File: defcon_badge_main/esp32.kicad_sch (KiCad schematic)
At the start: 15 parts, among them J1 USB_C_Receptacle, SW1 Push_Button, SW2 Push_Button, U3 ESP32-C5-WROOM-1U

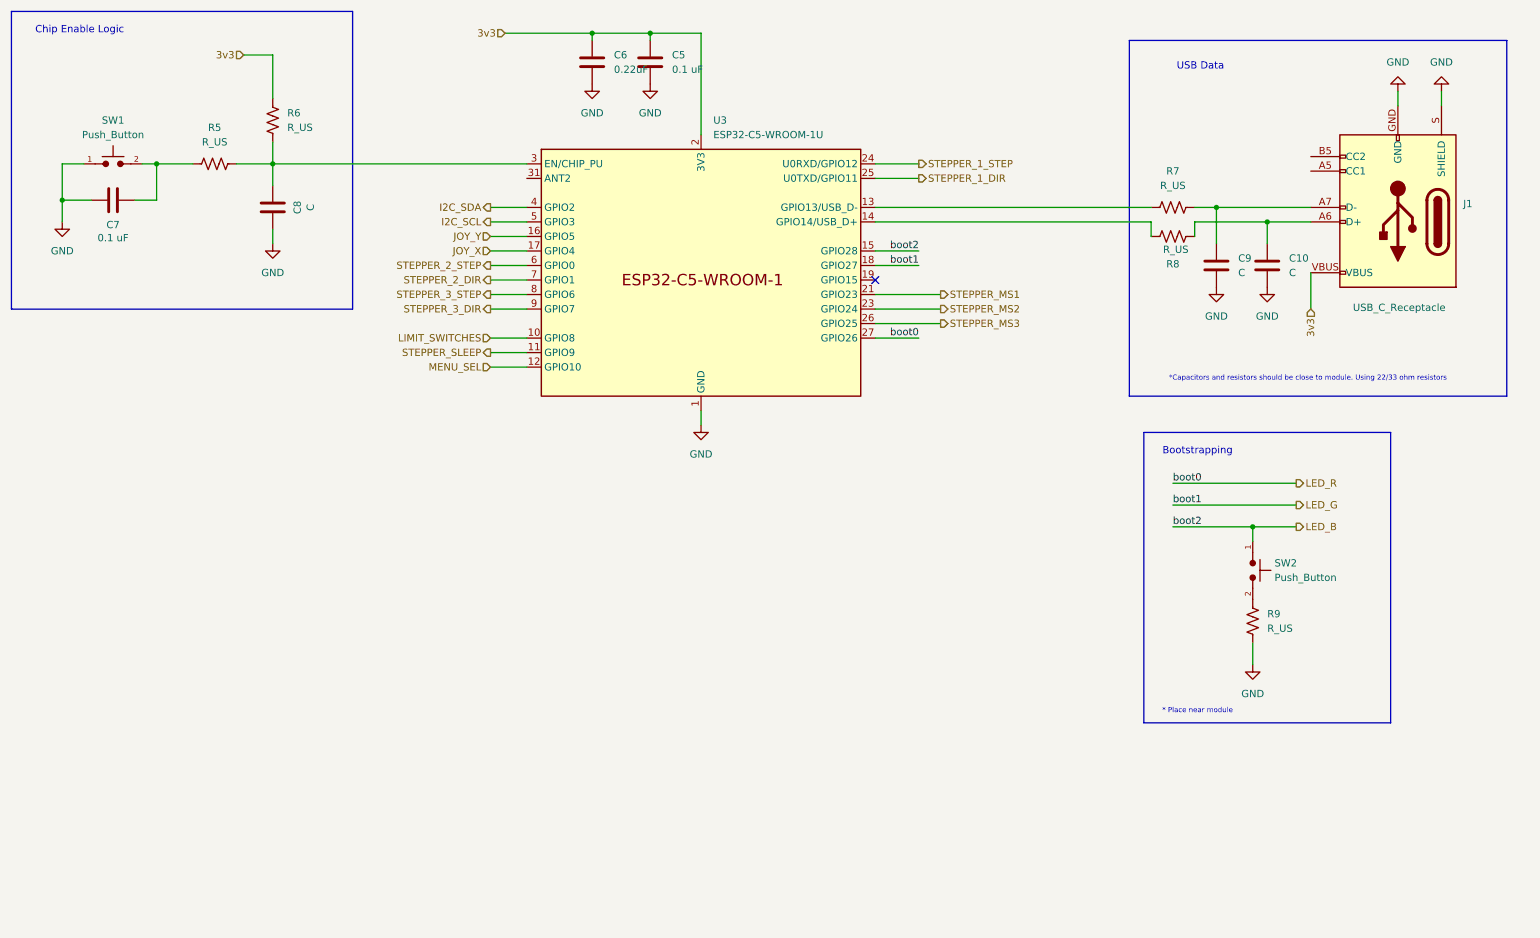
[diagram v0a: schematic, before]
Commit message: ESP32 test board layout
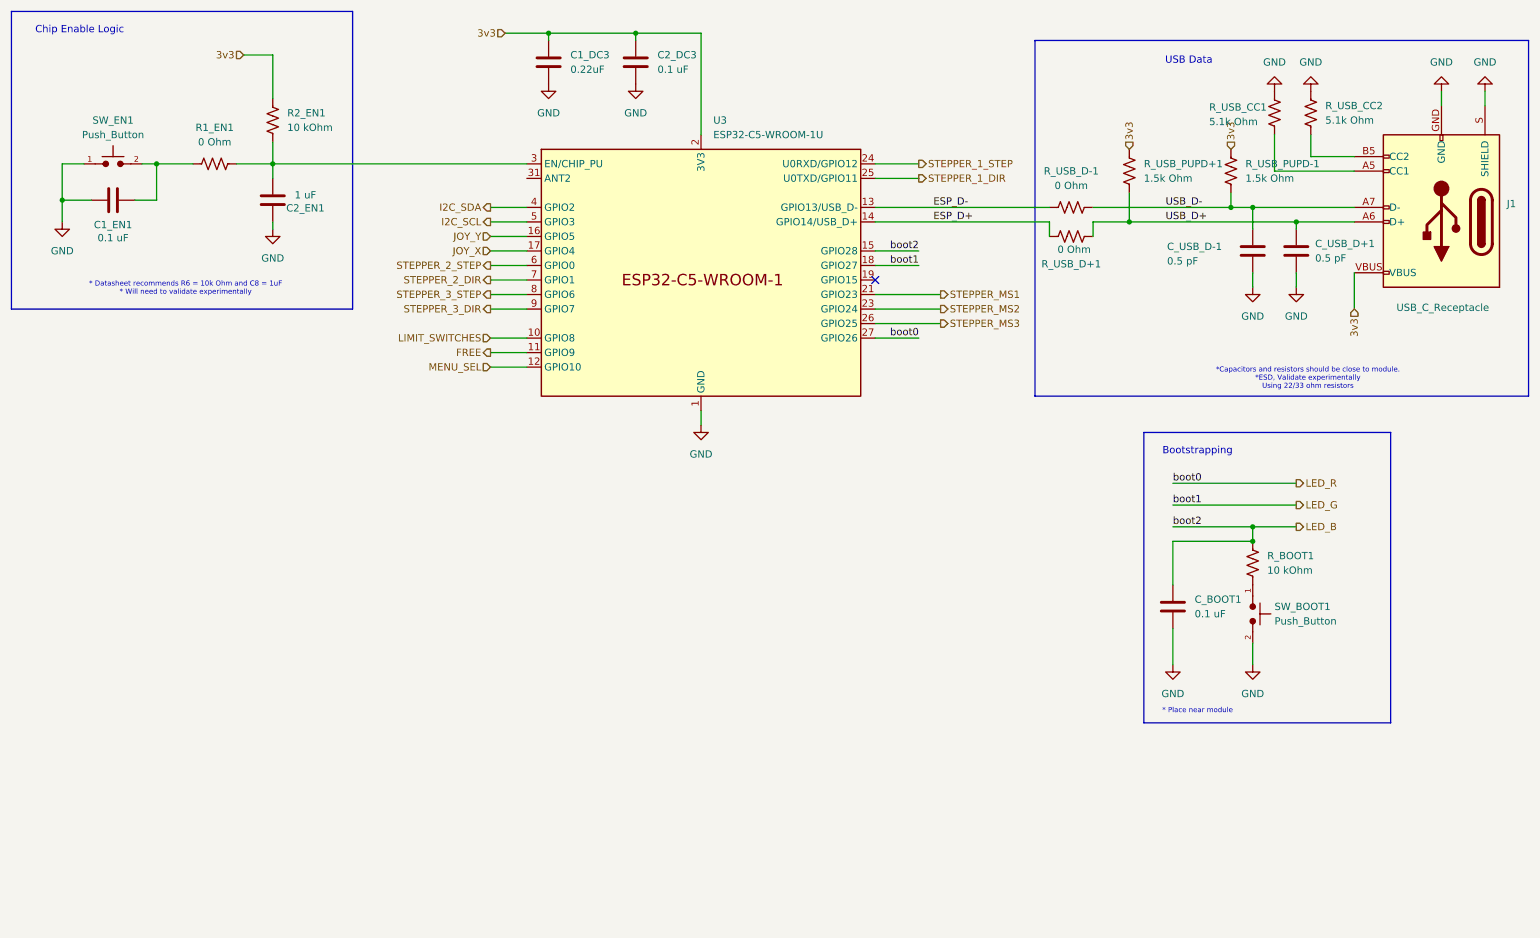
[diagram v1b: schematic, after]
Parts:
- added C_BOOT1: 0.1 uF, PCM_SparkFun-Coil:0805, symbol Device:C
- added R_USB_CC1, R_USB_CC2: 5.1k Ohm, PCM_SparkFun-Coil:0805, symbol Device:R_US
- added R_USB_PUPD+1, R_USB_PUPD-1: 1.5k Ohm, PCM_SparkFun-Coil:0805, symbol Device:R_US
- C1_DC3: renamed from C6; footprint (none) -> PCM_SparkFun-Coil:0805
- C1_EN1: renamed from C7; footprint (none) -> PCM_SparkFun-Coil:0805
- C2_DC3: renamed from C5; footprint (none) -> PCM_SparkFun-Coil:0805
- C2_EN1: renamed from C8; value C -> 1 uF; footprint (none) -> PCM_SparkFun-Coil:0805
- C_USB_D+1: renamed from C10; value C -> 0.5 pF; footprint (none) -> Capacitor_SMD:C_0402_1005Metric
- C_USB_D-1: renamed from C9; value C -> 0.5 pF; footprint (none) -> Capacitor_SMD:C_0402_1005Metric
- R1_EN1: renamed from R5; value R_US -> 0 Ohm; footprint (none) -> PCM_SparkFun-Coil:0805
- R2_EN1: renamed from R6; value R_US -> 10 kOhm; footprint (none) -> PCM_SparkFun-Coil:0805
- R_BOOT1: renamed from R9; value R_US -> 10 kOhm; footprint (none) -> PCM_SparkFun-Fuse:1206
- R_USB_D+1: renamed from R8; value R_US -> 0 Ohm; footprint (none) -> PCM_SparkFun-Coil:0805
- R_USB_D-1: renamed from R7; value R_US -> 0 Ohm; footprint (none) -> PCM_SparkFun-Coil:0805
- SW_BOOT1: renamed from SW2; footprint Button_Switch_THT:SW_PUSH_6mm -> Button_Switch_SMD:SW_SPST_PTS645
- SW_EN1: renamed from SW1; footprint Button_Switch_THT:SW_PUSH_6mm -> Button_Switch_SMD:SW_SPST_PTS645
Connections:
- net 3v3: now also R_USB_PUPD+1.2, R_USB_PUPD-1.2
- net GND: now also SW_BOOT1.2, C_BOOT1.2, R_USB_CC1.1, R_USB_CC2.2; no longer R_BOOT1.1
- net LED_B: now also R_BOOT1.2, C_BOOT1.1; no longer SW_BOOT1.1
- net at J1.A5 (CC1): now also R_USB_CC1.2
- net USB_D+: now reaches C_USB_D+1.1, J1.A6 (D+), J1.B6 (D+), R_USB_D+1.1
- net USB_D+: now also R_USB_PUPD+1.1
- net USB_D-: now reaches C_USB_D-1.1, J1.A7 (D-), J1.B7 (D-), R_USB_D-1.2
- net USB_D-: now also R_USB_PUPD-1.1
- net at J1.B5 (CC2): now also R_USB_CC2.1
- net ESP_D+: now reaches R_USB_D+1.2, U3.14 (GPIO14/USB_D+)
- net ESP_D-: now reaches R_USB_D-1.1, U3.13 (GPIO13/USB_D-)
- net STEPPER_SLEEP renamed FREE
- new net: R_BOOT1.1, SW_BOOT1.1
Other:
- note added: "* Datasheet recommends R6 = 10k Ohm and C8 = 1uF * Will need to validate experimentally"
- note added: "*Capacitors and resistors should be close to module. *ESD, Validate experimentally Using 22/33 ohm resistors"
- note removed: "*Capacitors and resistors should be close to module. Using 22/33 ohm resistors"
- moved on the sheet: C1_DC3, C2_DC3, C2_EN1, C_USB_D+1, C_USB_D-1, J1, R_BOOT1, R_USB_D+1, R_USB_D-1, SW_BOOT1

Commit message: begin full layout
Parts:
- added D1, D2: PESD0402, PCM_SparkFun-Capacitor:C_0402_1005Metric, symbol PCM_SparkFun-DiscreteSemi:D_TVS_0402_14V
- R_BOOT1: footprint PCM_SparkFun-Fuse:1206 -> PCM_SparkFun-Coil:0805
- R_USB_D+1, R_USB_D-1, R_USB_PUPD+1, R_USB_PUPD-1: footprint PCM_SparkFun-Coil:0805 -> Resistor_SMD:R_0402_1005Metric
- SW_BOOT1, SW_EN1: footprint Button_Switch_SMD:SW_SPST_PTS645 -> Button_Switch_SMD:SW_SPST_PTS810
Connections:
- net GND: now also D1.1 (A1), D2.1 (A1)
- net USB_D+: now also D1.2 (A2)
- net USB_D-: now also D2.2 (A2)
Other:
- note added: "*Capacitors and resistors should be close to module. *ESD, Validate experimentally Using 22/33 ohm resistors ESD protection diodes should be near connector"
- note removed: "*Capacitors and resistors should be close to module. *ESD, Validate experimentally Using 22/33 ohm resistors"
- moved on the sheet: C1_DC3, C2_DC3, C_BOOT1, C_USB_D+1, C_USB_D-1, J1, R_BOOT1, R_USB_CC1, R_USB_CC2, R_USB_D+1, R_USB_D-1, R_USB_PUPD+1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

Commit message: more layout
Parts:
- C1_DC3, C1_EN1, C2_DC3, C2_EN1, C_BOOT1, R1_EN1, R2_EN1, R_BOOT1, R_USB_CC1, R_USB_CC2: footprint PCM_SparkFun-Coil:0805 -> joystick:R_0805_2012Metric_Pad1.20x1.40mm_HandSolder_MINE
- C_USB_D+1, C_USB_D-1: footprint Capacitor_SMD:C_0402_1005Metric -> joystick:R_0402_1005Metric_Pad0.72x0.64mm_HandSolder_MINE
- D1, D2: footprint PCM_SparkFun-Capacitor:C_0402_1005Metric -> joystick:R_0402_1005Metric_Pad0.72x0.64mm_HandSolder_MINE
- R_USB_D+1, R_USB_D-1, R_USB_PUPD+1, R_USB_PUPD-1: footprint Resistor_SMD:R_0402_1005Metric -> joystick:R_0402_1005Metric_Pad0.72x0.64mm_HandSolder_MINE
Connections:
- net JOY_X: now also U3.16 (GPIO5); no longer U3.17 (GPIO4)
- net JOY_Y: now also U3.17 (GPIO4); no longer U3.16 (GPIO5)
- net LIMIT_SWITCHES: now also U3.6 (GPIO0); no longer U3.10 (GPIO8)
- net STEPPER_1_DIR: now also U3.24 (U0RXD/GPIO12); no longer U3.25 (U0TXD/GPIO11)
- net STEPPER_1_STEP: now also U3.25 (U0TXD/GPIO11); no longer U3.24 (U0RXD/GPIO12)
- net STEPPER_2_DIR: now also U3.9 (GPIO7); no longer U3.7 (GPIO1)
- net STEPPER_2_STEP: now also U3.10 (GPIO8); no longer U3.6 (GPIO0)
- net STEPPER_3_DIR: now also U3.7 (GPIO1); no longer U3.9 (GPIO7)
- net EN: now reaches C2_EN1.1, R1_EN1.2, R2_EN1.1, U3.3 (EN/CHIP_PU)
- net SW_EN: now reaches C1_EN1.1, R1_EN1.1, SW_EN1.2
- net boot2_sw: now reaches R_BOOT1.1, SW_BOOT1.1
- net ESP_D+ renamed ESP_D_P
- net ESP_D- renamed ESP_D_N
- net USB_D+ renamed USB_D_P
- net USB_D- renamed USB_D_N
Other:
- moved on the sheet: SW_BOOT1

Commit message: moar layout
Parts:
- removed J1: USB_C_Receptacle, PCM_SparkFun-Connector:USB-C_16, symbol PCM_SparkFun-Connector:USB_C_Receptacle
- removed R_USB_CC1, R_USB_CC2: 5.1k Ohm, joystick:R_0805_2012Metric_Pad1.20x1.40mm_HandSolder_MINE, symbol Device:R_US
- added U1: ~, joystick:usb_typea_boardedge, symbol joystick:usb_typa_boardedge
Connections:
- net GND: now also U1.4 (GND)
- net USB_D_N: now also U1.2 (D-)
- net USB_D_P: now also U1.3 (D+)
- new net 5v: U1.1 (+5V)

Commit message: added component parts and modifications
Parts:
- C1_DC3: MPN (none) -> GMC10X5R224K25NT; Rating (none) -> 16V
- C1_EN1, C2_DC3, C_BOOT1: footprint joystick:R_0805_2012Metric_Pad1.20x1.40mm_HandSolder_MINE -> joystick:R_0603_1608Metric_Pad0.98x0.95mm_HandSolder_MINE; MPN (none) -> GMC10X7R104M16NTD; Rating (none) -> 16V
- C2_EN1: MPN (none) -> GMC21X5R105K16NT
- C_USB_D+1, C_USB_D-1: MPN (none) -> GMC04CG0R5C50NT; Rating (none) -> 16V
- D1, D2: MPN (none) -> CES10402V05B0DG
- R1_EN1: footprint joystick:R_0805_2012Metric_Pad1.20x1.40mm_HandSolder_MINE -> joystick:R_0603_1608Metric_Pad0.98x0.95mm_HandSolder_MINE; MPN (none) -> RM06J000CT
- R2_EN1, R_BOOT1: MPN (none) -> RM10F1002CT; TOL (none) -> 1%
- R_USB_D+1, R_USB_D-1: MPN (none) -> RM04J000CT
- R_USB_PUPD+1, R_USB_PUPD-1: MPN (none) -> RM04J152CT
- SW_BOOT1, SW_EN1, U1: now not fitted
- U3: MPN (none) -> ESP32-C5-WROOM-1U-N8R8
